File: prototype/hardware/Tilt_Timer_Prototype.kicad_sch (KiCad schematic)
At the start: 11 parts, among them J1 Conn_02x07_Counter_Clockwise, Q1 PNP, Q2 PNP, Q3 PNP, Q4 PNP, U2 MPU6050 Module, U3 74HC595

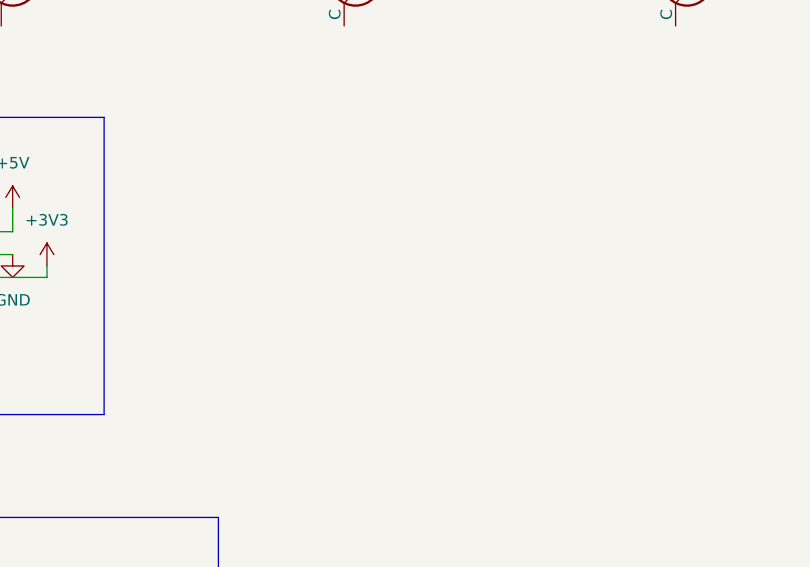
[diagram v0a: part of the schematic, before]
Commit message: created new symbol for xiao esp32 c6 and added to schematic
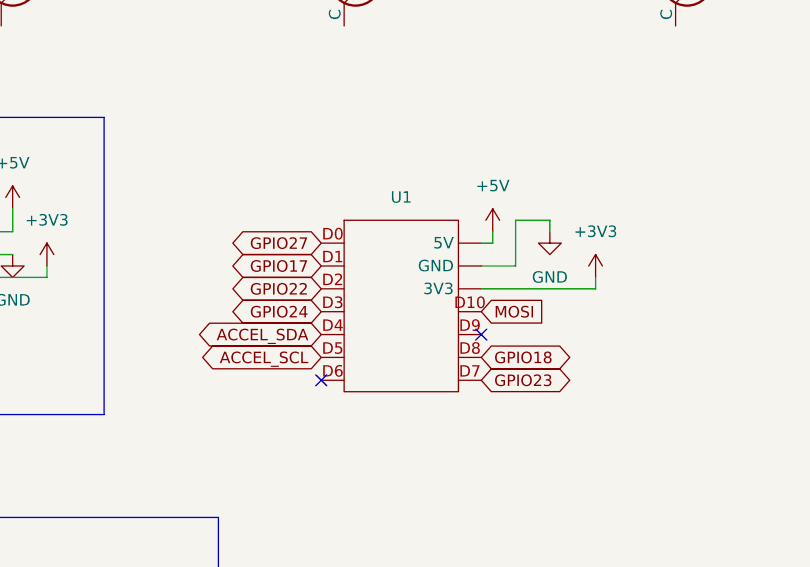
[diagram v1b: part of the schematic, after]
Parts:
- added U1: (no value), symbol Prototype_Parts:Xiao_ESP32_C6
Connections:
- net +3V3: now also U1. (3V3)
- net +5V: now also U1. (3V3)
- net ACCEL_SCL: now also U1.D5
- net ACCEL_SDA: now also U1.D4
- net GND: now also U1. (3V3)
- net GPIO17: now also U1.D1
- net GPIO18: now also U1.D8
- net GPIO22: now also U1.D2
- net GPIO23: now also U1.D7
- net GPIO24: now also U1.D3
- net GPIO27: now also U1.D0
- net MOSI: now also U1.D10
- no-connect marks 3 -> 5

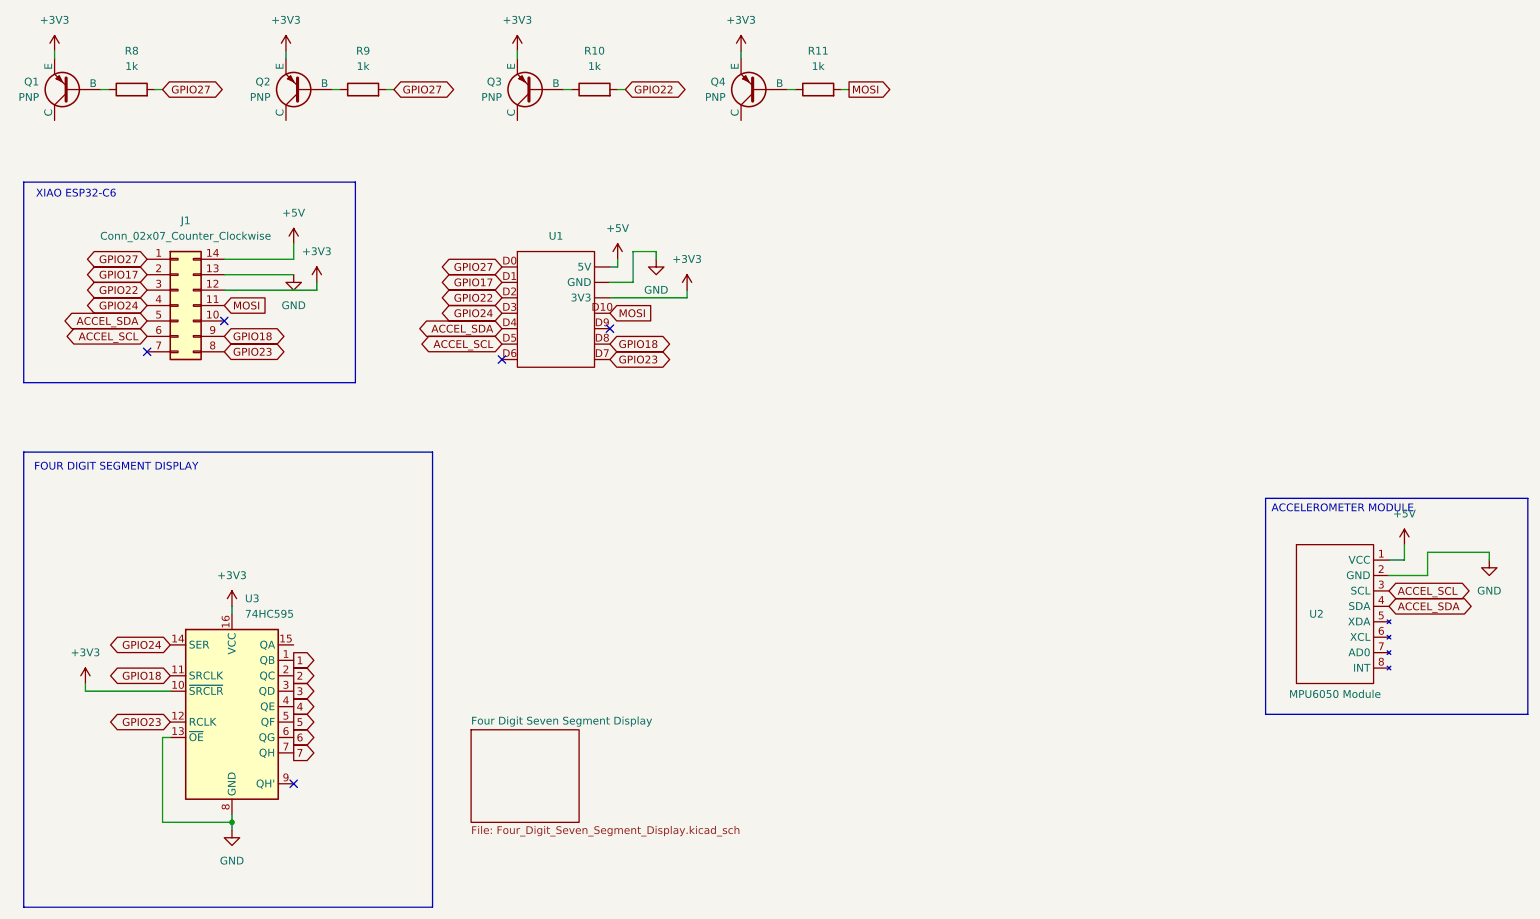
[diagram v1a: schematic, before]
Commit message: corrected and increased readability of symbol, updated esp32 section in schematic
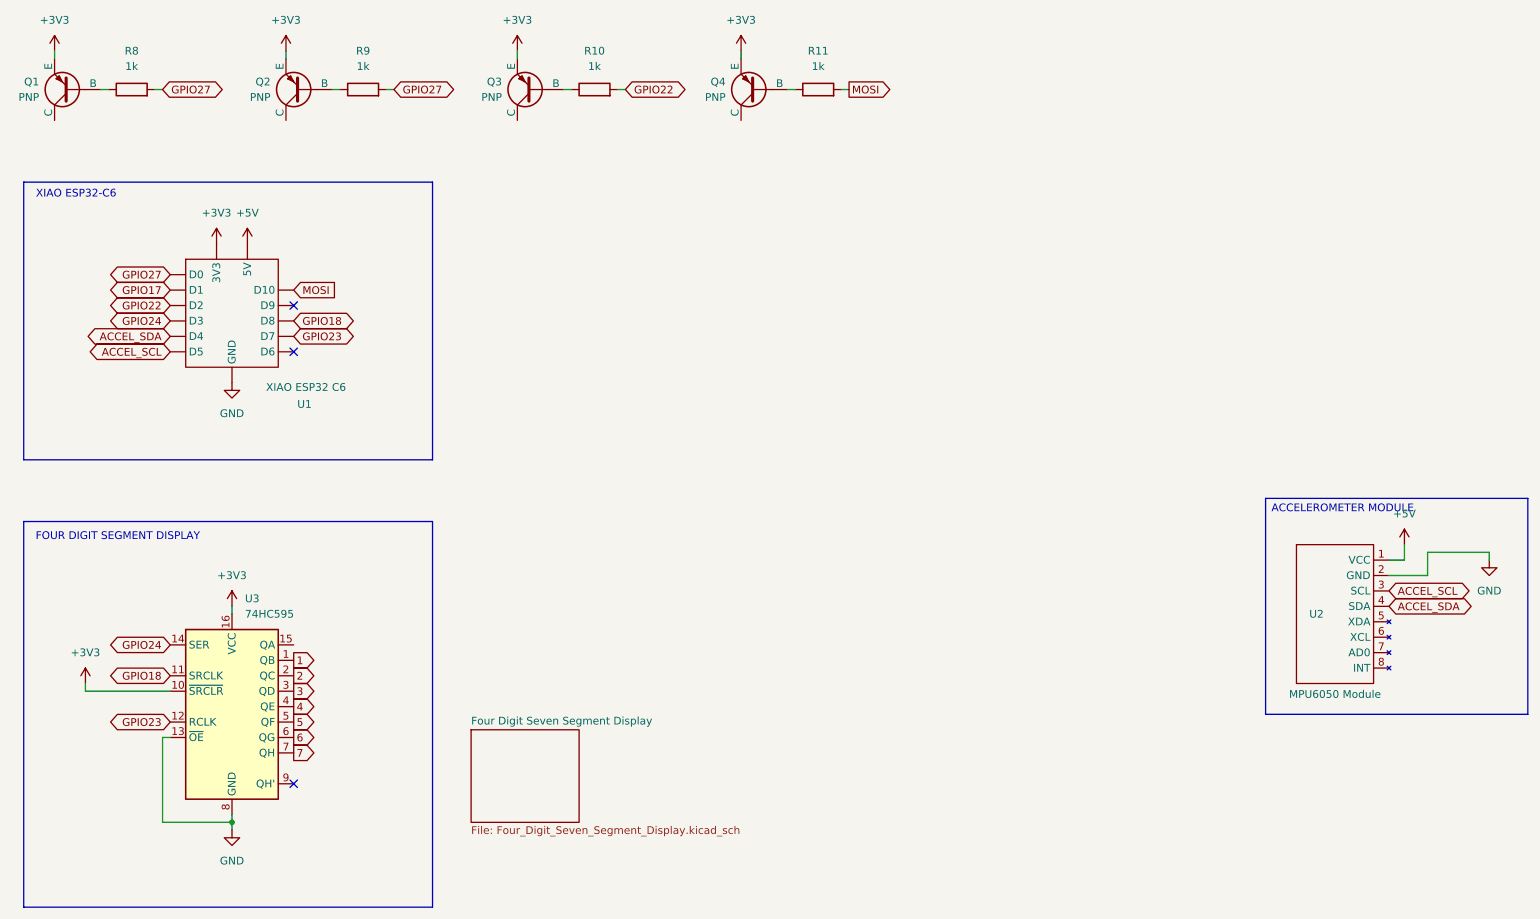
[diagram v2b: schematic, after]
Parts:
- removed J1: Conn_02x07_Counter_Clockwise, symbol Connector_Generic:Conn_02x07_Counter_Clockwise
- U1: value (none) -> XIAO ESP32 C6
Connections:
- net ACCEL_SCL: now also U1. (D6); no longer U1.D5
- net ACCEL_SDA: now also U1. (D6); no longer U1.D4
- net GPIO17: now also U1. (D6); no longer U1.D1
- net GPIO18: now also U1. (D6); no longer U1.D8
- net GPIO22: now also U1. (D6); no longer U1.D2
- net GPIO23: now also U1. (D6); no longer U1.D7
- net GPIO24: now also U1. (D6); no longer U1.D3
- net GPIO27: now also U1. (D6); no longer U1.D0
- net MOSI: now also U1. (D6); no longer U1.D10
- no-connect marks 5 -> 3
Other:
- moved on the sheet: U1
